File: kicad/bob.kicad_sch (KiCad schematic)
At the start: 53 parts, among them J1 Mini USB Female, J2 GPIO (Optional), J3 GPIO (Optional), J4 Battery Connector, J5 Conn_01x03_Male, SW1 Screw Switch, U1 W25Q64JVSS, U2 AMS1117-3.3, Y1 12MHz

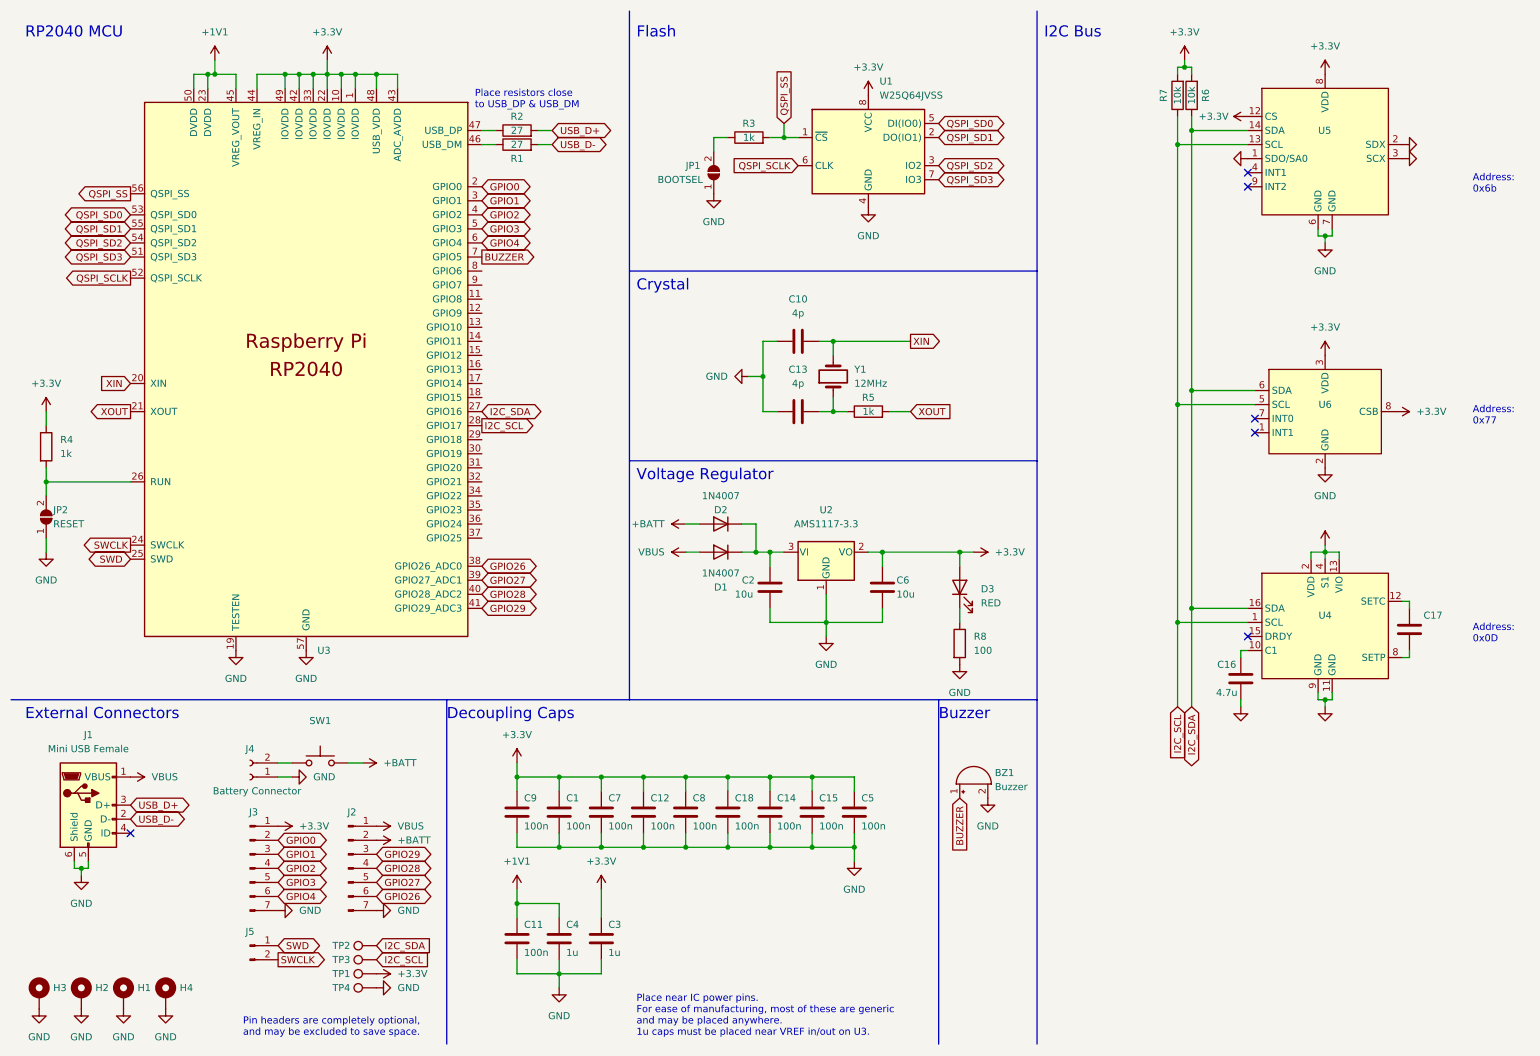
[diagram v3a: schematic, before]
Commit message: Fixed very minor alignment issue that was annoying me.
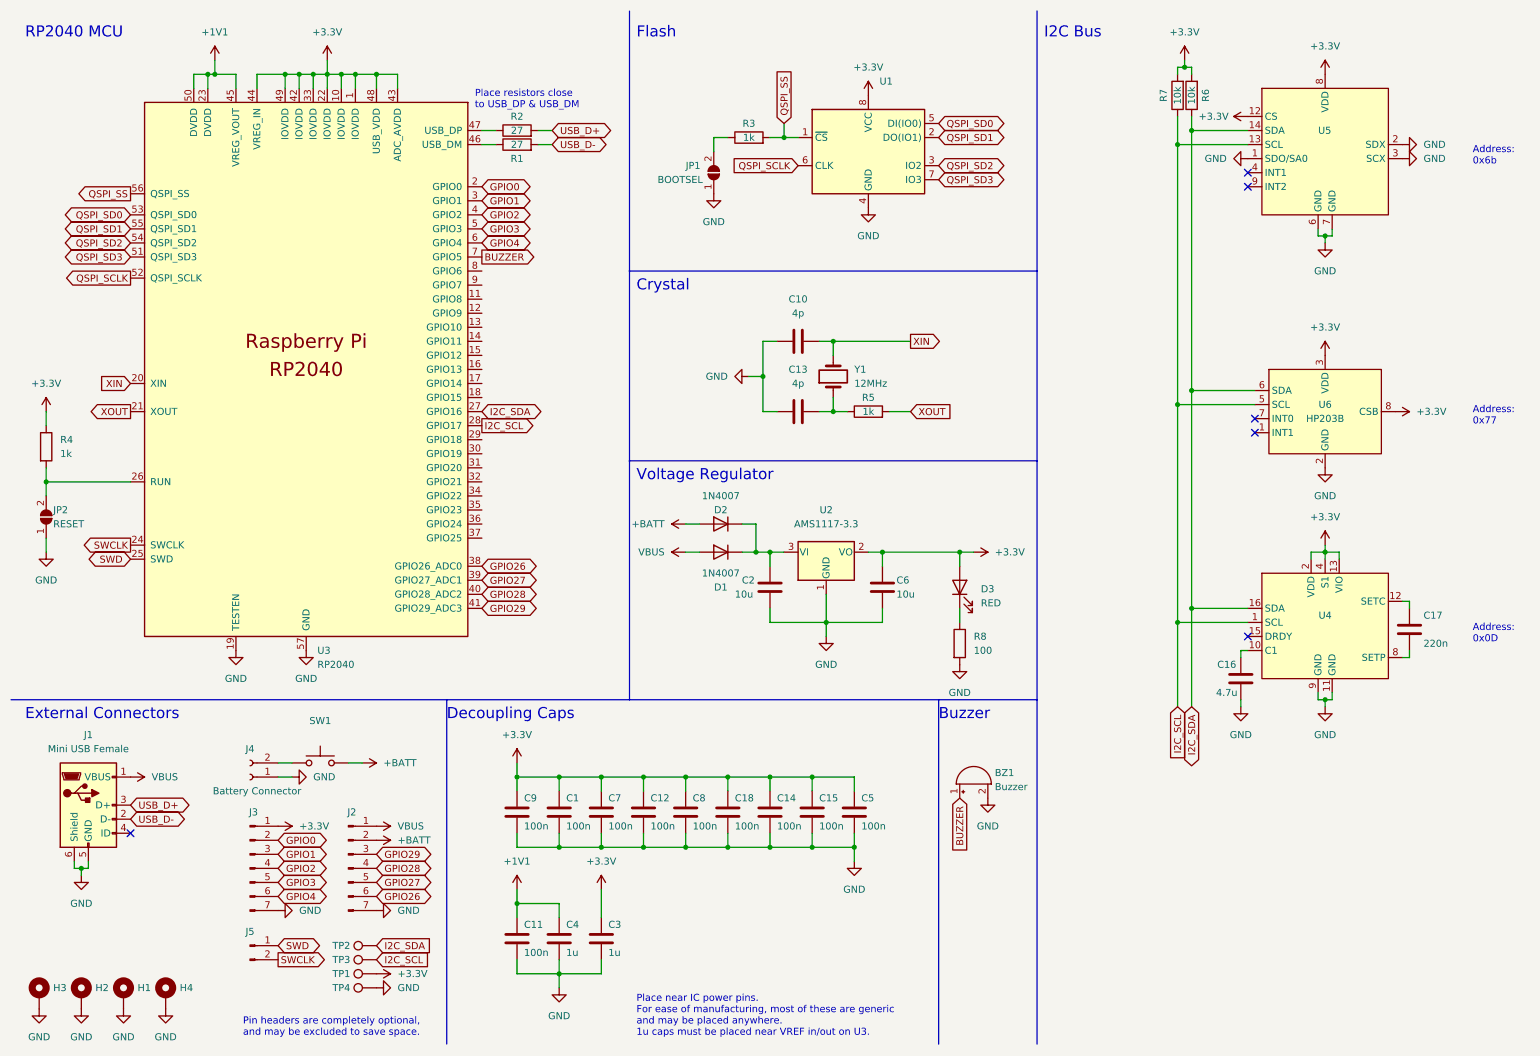
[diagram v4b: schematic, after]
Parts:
- C17: value (none) -> 220n
- U1: value W25Q64JVSS -> (none)
- U3: value (none) -> RP2040
- U4: footprint (none) -> YAR_Sensors:QMC5883L-LGA16
- U5: footprint (none) -> YAR_Sensors:QMI8658C-LGA14
- U6: value (none) -> HP203B; footprint (none) -> YAR_Sensors:HP203B-LGA8
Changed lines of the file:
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@@
     (effects (font (size 1.27 1.27)) (justify left bottom))
   )
-  (text "Address:\n0x6b" (at 274.32 44.45 0)
+  (text "Address:\n0x6b" (at 274.32 39.37 0)
     (effects (font (size 1.27 1.27)) (justify left bottom))
   )
@@
       (effects (font (size 1.27 1.27)) hide)
     )
-    (property "Value" "" (id 1) (at 265.43 35.5599 90)
+    (property "Value" "GND" (id 1) (at 265.43 35.5599 90)
       (effects (font (size 1.27 1.27)) (justify right))
     )
@@
       (effects (font (size 1.27 1.27)) hide)
     )
-    (property "Value" "" (id 1) (at 232.41 142.24 0))
+    (property "Value" "GND" (id 1) (at 232.41 142.24 0))
     (property "Footprint" "" (id 2) (at 232.41 137.16 0)
       (effects (font (size 1.27 1.27)) hide)
@@
       (effects (font (size 1.27 1.27)) (justify left))
     )
-    (property "Value" "W25Q64JVSS" (id 1) (at 167.1194 26.67 0)
+    (property "Value" "" (id 1) (at 167.1194 26.67 0)
       (effects (font (size 1.27 1.27)) (justify left))
     )
@@
       (effects (font (size 1.27 1.27)) hide)
     )
-    (property "Value" "" (id 1) (at 247.65 142.24 0))
+    (property "Value" "GND" (id 1) (at 247.65 142.24 0))
     (property "Footprint" "" (id 2) (at 247.65 137.16 0)
       (effects (font (size 1.27 1.27)) hide)
@@
       (effects (font (size 1.27 1.27)) hide)
     )
-    (property "Value" "" (id 1) (at 247.65 102.87 0))
+    (property "Value" "+3.3V" (id 1) (at 247.65 102.87 0))
     (property "Footprint" "" (id 2) (at 247.65 107.95 0)
       (effects (font (size 1.27 1.27)) hide)
@@
     )
     (property "Value" "" (id 1) (at 247.65 35.56 0))
-    (property "Footprint" "" (id 2) (at 247.65 34.29 0)
+    (property "Footprint" "YAR_Sensors:QMI8658C-LGA14" (id 2) (at 247.65 34.29 0)
       (effects (font (size 1.27 1.27)) hide)
     )
@@
       (effects (font (size 1.27 1.27)) (justify right))
     )
-    (property "Value" "" (id 1) (at 265.43 125.73 0)
+    (property "Value" "220n" (id 1) (at 265.43 125.73 0)
       (effects (font (size 1.27 1.27)) (justify right))
     )
@@
       (effects (font (size 1.27 1.27)) hide)
     )
-    (property "Value" "" (id 1) (at 229.87 38.0999 90)
+    (property "Value" "GND" (id 1) (at 229.87 38.0999 90)
       (effects (font (size 1.27 1.27)) (justify right))
     )
@@
     (in_bom yes) (on_board yes)
     (property "Reference" "U6" (id 0) (at 247.65 82.55 0))
-    (property "Value" "" (id 1) (at 247.65 85.09 0))
-    (property "Footprint" "" (id 2) (at 247.65 83.82 0)
+    (property "Value" "HP203B" (id 1) (at 247.65 85.09 0))
+    (property "Footprint" "YAR_Sensors:HP203B-LGA8" (id 2) (at 247.65 83.82 0)
       (effects (font (size 1.27 1.27)) hide)
     )
@@
     (property "Reference" "U4" (id 0) (at 247.65 120.65 0))
     (property "Value" "" (id 1) (at 247.65 123.19 0))
-    (property "Footprint" "" (id 2) (at 247.65 107.95 0)
+    (property "Footprint" "YAR_Sensors:QMC5883L-LGA16" (id 2) (at 247.65 107.95 0)
       (effects (font (size 1.27 1.27)) hide)
     )
@@
       (effects (font (size 1.27 1.27)) hide)
     )
-    (property "Value" "" (id 1) (at 265.43 38.0999 90)
+    (property "Value" "GND" (id 1) (at 265.43 38.0999 90)
       (effects (font (size 1.27 1.27)) (justify right))
     )
@@
       (effects (font (size 1.27 1.27)) (justify left))
     )
-    (property "Value" "" (id 1) (at 65.5194 129.54 0)
-      (effects (font (size 1.27 1.27)) (justify left))
-    )
+    (property "Value" "RP2040" (id 1) (at 65.5194 129.54 0)
+      (effects (font (size 1.27 1.27)) (justify left))
+    )

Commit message: Added pyro channels Added bendy traces Added status LED Removed buzzer
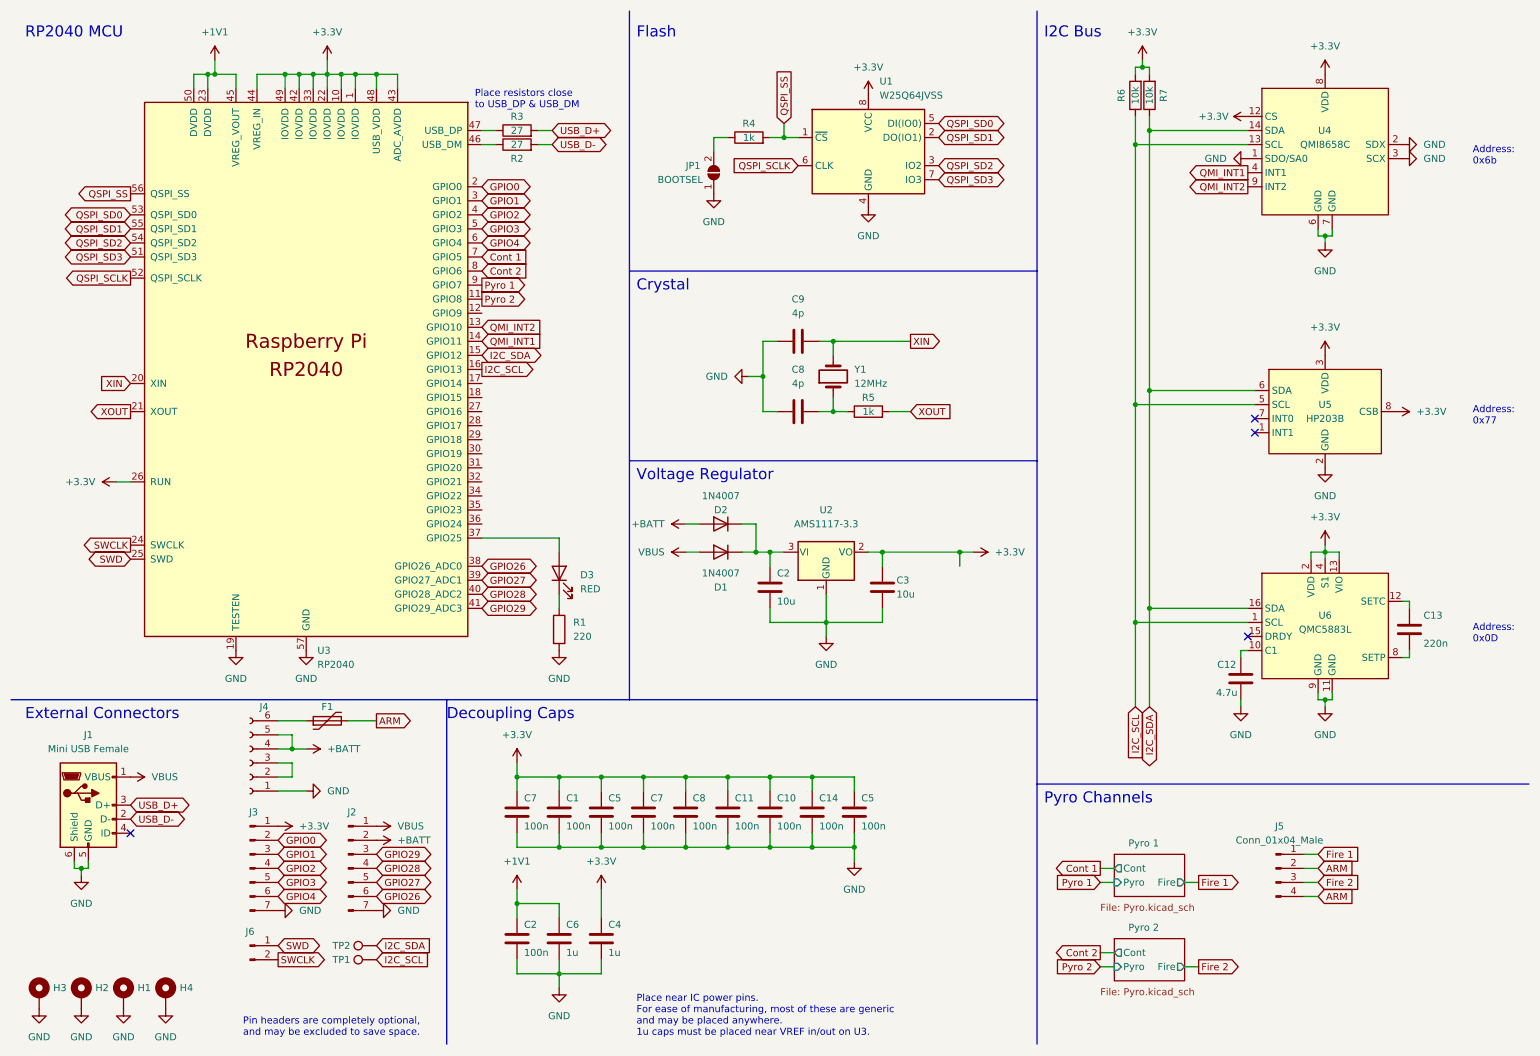
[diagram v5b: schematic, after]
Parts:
- removed BZ1: Buzzer, Buzzer_Beeper:Buzzer_12x9.5RM7.6, symbol Device:Buzzer
- removed J4: Battery Connector, Connector_Wire:Compact_Relief, symbol Connector:Conn_01x02_Female
- removed JP2: RESET, Jumper:SolderJumper-2_P1.3mm_Open_RoundedPad1.0x1.5mm, symbol Jumper:SolderJumper_2_Open
- removed R4: 1k, Resistor_SMD:R_0603_1608Metric, symbol Device:R
- removed R8: 100, Resistor_SMD:R_0603_1608Metric, symbol Device:R
- removed SW1: Screw Switch, Connector:Screw_Switch_M2, symbol Switch:SW_Push
- removed TP1, TP4: TestPoint, TestPoint:TestPoint_Pad_D1.0mm, symbol Connector:TestPoint
- added F1: Polyfuse, Fuse:Fuse_0603_1608Metric, symbol Device:Polyfuse
- added J4: Screw Terminal, 2.54mm, YAR_Connectors:ScrewTerm_2.54x06, symbol Connector:Conn_01x06_Female
- added J5: Conn_01x04_Male, YAR_Connectors:ScrewTerm_2.54x04, symbol Connector:Conn_01x04_Male
- added R1: 220, Resistor_SMD:R_0603_1608Metric, symbol Device:R
- D3: footprint LED_THT:LED_D3.0mm -> LED_SMD:LED_0603_1608Metric
- JP1: footprint Jumper:SolderJumper-2_P1.3mm_Open_RoundedPad1.0x1.5mm -> Button_Switch_SMD:SW_SPST_B3U-1000P
- U1: value (none) -> W25Q64JVSS
- U4: renamed from U5; value (none) -> QMI8658C
- U6: renamed from U4; value (none) -> QMC5883L
- renumbered C14 to C10, C18 to C11, C16 to C12, C17 to C13, C15 to C14, C11 to C2, C6 to C3, C3 to C4, C7 to C5, C4 to C6, C9 to C7, C12 to C7, C13 to C8, C10 to C9, J5 to J6, R1 to R2, R2 to R3, R3 to R4, R7 to R6, R6 to R7, TP3 to TP1, U6 to U5
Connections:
- net +3V3: now also U3.26 (RUN); no longer D3.2 (A)
- net +BATT: now also J4.4 (Pin_4), J4.5 (Pin_5)
- net GND: now also J4.1 (Pin_1), R1.2
- net I2C_SCL: now also U3.16 (GPIO13); no longer U3.28 (GPIO17)
- net I2C_SDA: now also U3.15 (GPIO12); no longer U3.27 (GPIO16)
- net at D3.1 (K): now also R1.1
- net QMI_INT1: now reaches U4.4 (INT1)
- net QMI_INT1: now also U3.14 (GPIO11)
- net QMI_INT2: now reaches U4.9 (INT2)
- net QMI_INT2: now also U3.13 (GPIO10)
- net Pyro 2: now reaches U3.11 (GPIO8)
- net at U3.37 (GPIO25): now also D3.2 (A)
- net Cont 2: now reaches U3.8 (GPIO6)
- net Pyro 1: now reaches U3.9 (GPIO7)
- net BUZZER renamed Cont 1
- new net: J4.2 (Pin_2), J4.3 (Pin_3)
- new net: F1.1, J4.6 (Pin_6)
- new net ARM: F1.2, J5.2 (Pin_2), J5.4 (Pin_4)
- new net Fire 1: J5.1 (Pin_1)
- new net Fire 2: J5.3 (Pin_3)
- no-connect marks 6 -> 4
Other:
- added sheet Pyro 1 (Pyro.kicad_sch)
- added sheet Pyro 2 (Pyro.kicad_sch)
- note added: "Pyro Channels"
- note removed: "Buzzer"
- moved on the sheet: R6, R7
